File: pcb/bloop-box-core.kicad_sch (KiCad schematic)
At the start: 30 parts, among them J1 Raspberry_Pi_Header, J2 USB_C_Receptacle_USB2.0_16P, J4 Micro_SD_Card_Det1, SW1 Reset, SW2 Boot, U1 ESP32-C5-WROOM-1U, U2 AMS1117-3.3, U3 74LVC125APW

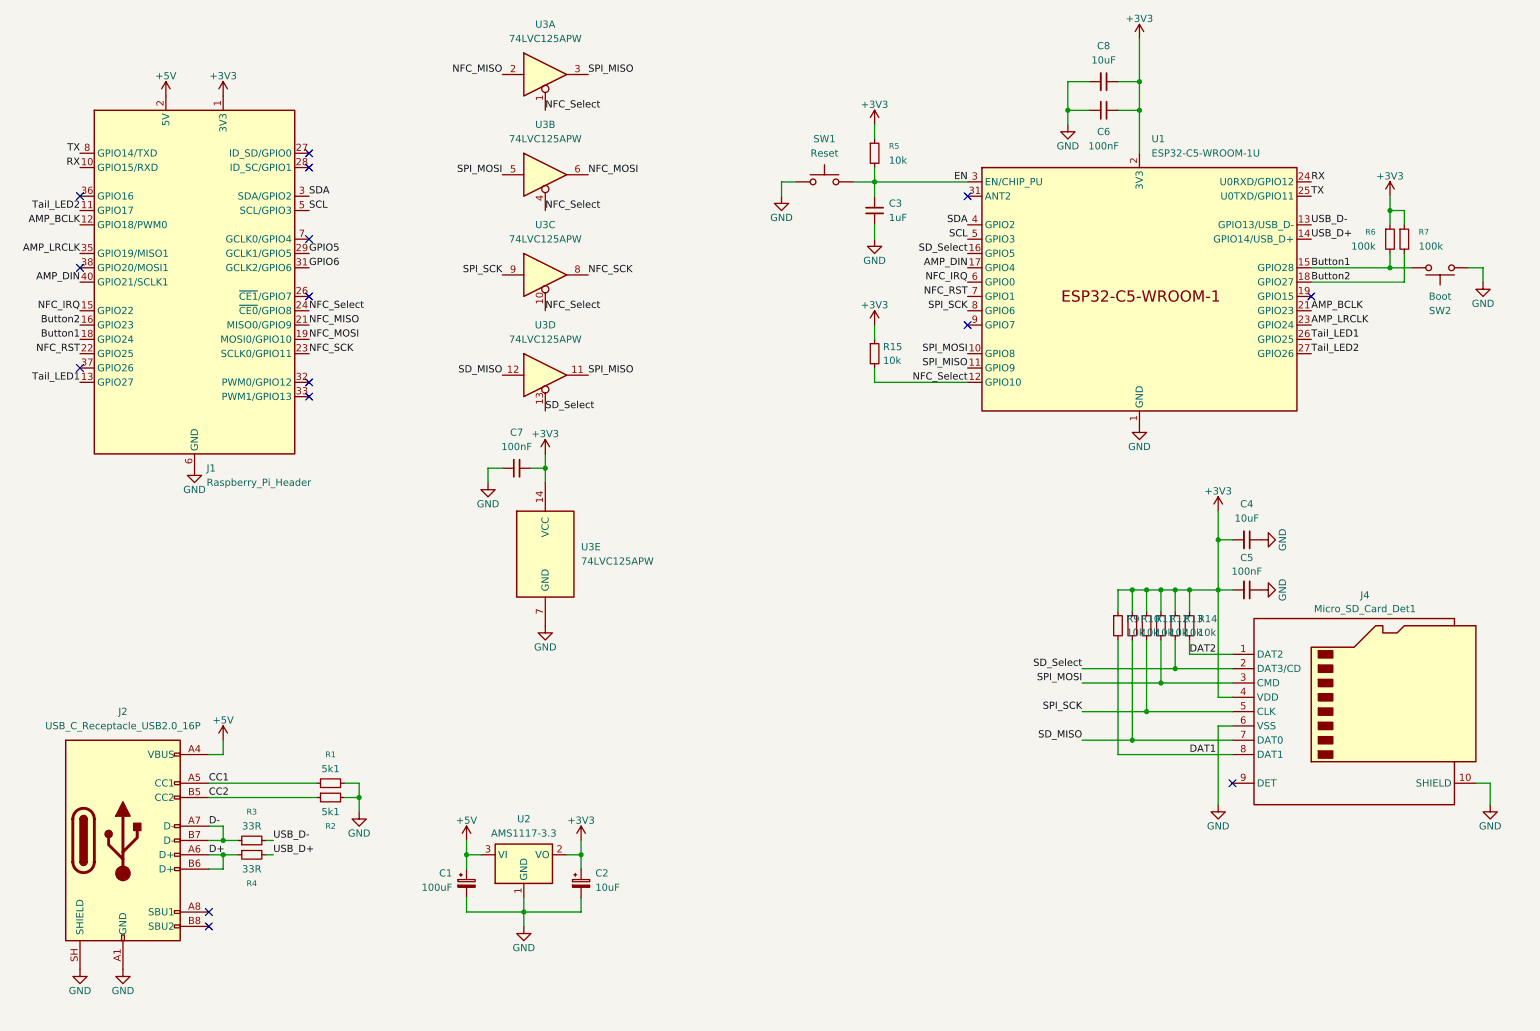
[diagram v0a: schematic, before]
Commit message: feat: trace-routing
All traces are routed
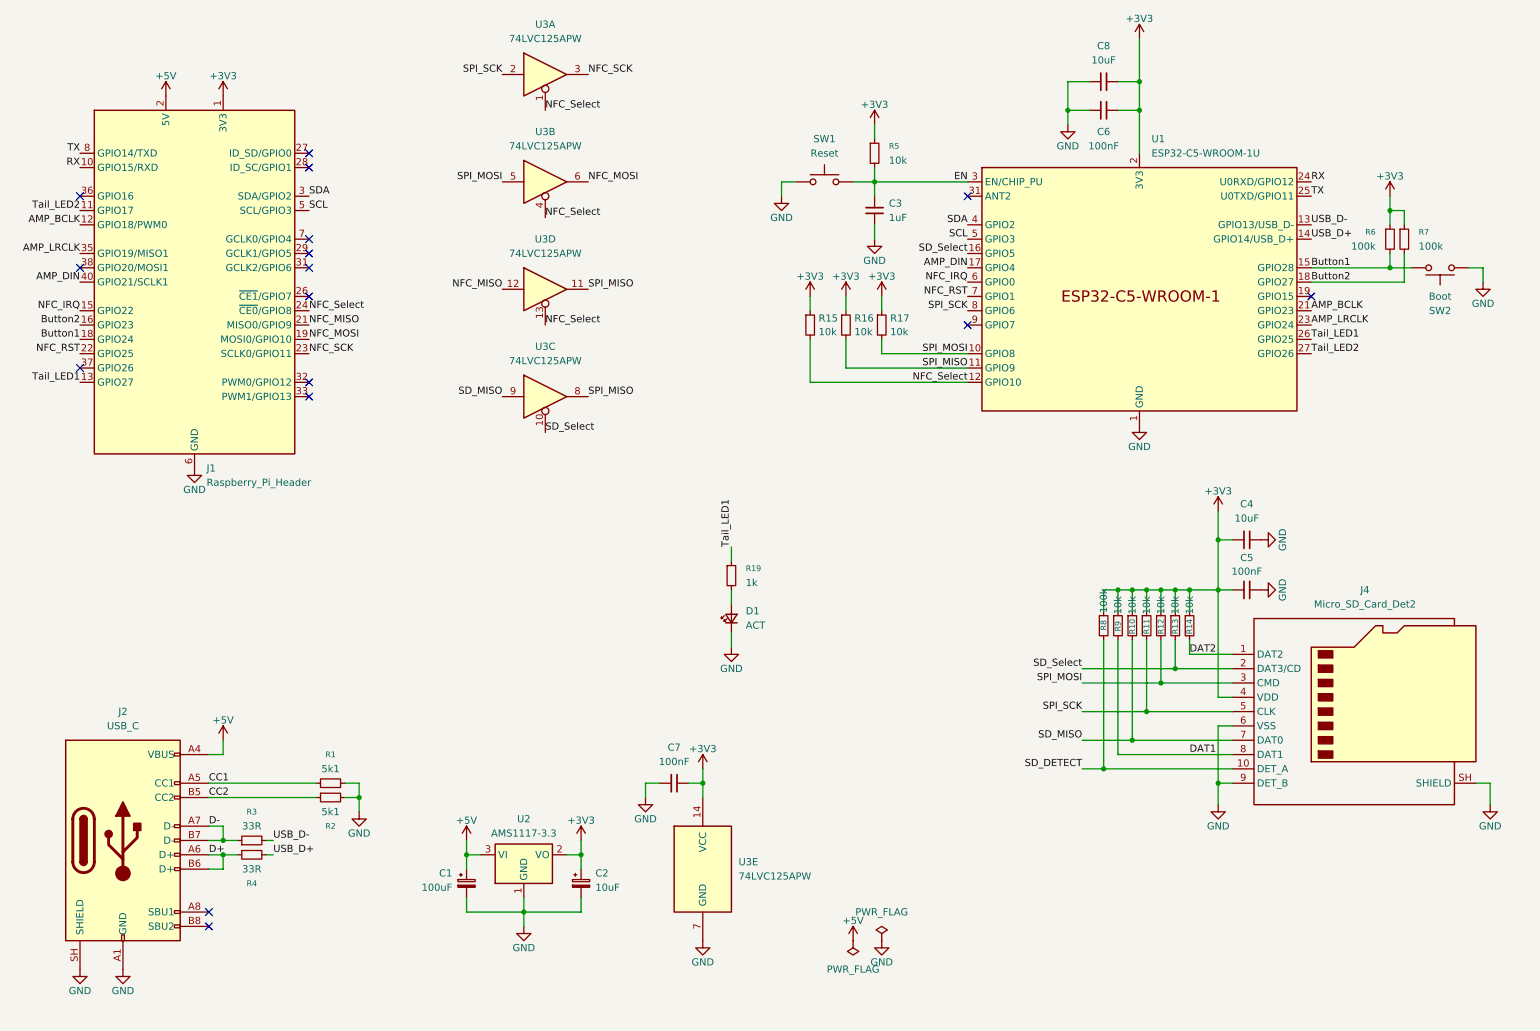
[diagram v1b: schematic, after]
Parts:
- added D1: ACT, LED_SMD:LED_0603_1608Metric, symbol Device:LED_Small
- added R16, R17: 10k, Resistor_SMD:R_0402_1005Metric, symbol Device:R_Small
- added R19: 1k, Resistor_SMD:R_0402_1005Metric, symbol Device:R_Small
- added R8: 100k, Resistor_SMD:R_0402_1005Metric, symbol Device:R_Small
- J2: value USB_C_Receptacle_USB2.0_16P -> USB_C
- J4: value Micro_SD_Card_Det1 -> Micro_SD_Card_Det2; footprint My_Footprints:TF_PUSH_Micro-SD-Connector -> Connector_Card:microSD_HC_Molex_104031-0811; symbol Connector:Micro_SD_Card_Det1 -> Connector:Micro_SD_Card_Det2; LCSC C393941 -> C585350
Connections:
- net +3V3: now also R16.1, R17.1, R8.1
- net GND: now also J4.9 (DET_B), J4.SH (SHIELD), D1.1 (K); no longer J4.10 (SHIELD)
- net NFC_MISO: now also U3.12; no longer U3.2
- net NFC_SCK: now also U3.3; no longer U3.8
- net NFC_Select: now also U3.13; no longer U3.10
- net SD_MISO: now also U3.9; no longer U3.12
- net SD_Select: now also U3.10; no longer U3.13
- net SPI_MISO: now also U3.8, R16.2; no longer U3.3
- net SPI_MOSI: now also R17.2
- net SPI_SCK: now also U3.2; no longer U3.9
- net Tail_LED1: now also R19.1
- net GPIO5: no longer names the net of J1.29 (GCLK1/GPIO5)
- net GPIO6: no longer names the net of J1.31 (GCLK2/GPIO6)
- new net: D1.2 (A), R19.2
- new net SD_DETECT: J4.10 (DET_A), R8.2
- no-connect marks 15 -> 16
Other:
- moved on the sheet: C7, R15, U3B, U3C, U3D, U3E

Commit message: feat: add detect pin for SD-Card
connect SD-Detect to IO7

feat: bottom silkscreen
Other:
- moved on the sheet: C1, C2, C7, D1, R19, U2, U3A, U3B, U3C, U3D, U3E

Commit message: feat: add edge rails
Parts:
- renumbered R19 to R18
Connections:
- net SD_DETECT: now also U1.9 (GPIO7)
- no-connect marks 16 -> 15
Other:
- moved on the sheet: R15, R16, R17
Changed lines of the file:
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@@
 	)
 	(no_connect
-		(at 184.15 73.66)
-	)
-	(no_connect
 		(at 49.53 177.8)
 	)
@@
 	(wire
 		(pts
-			(xy 168.91 68.58) (xy 168.91 71.12)
+			(xy 167.64 68.58) (xy 167.64 71.12)
 		)
 		(stroke
@@
 	(wire
 		(pts
-			(xy 156.21 68.58) (xy 156.21 71.12)
+			(xy 154.94 68.58) (xy 154.94 71.12)
 		)
 		(stroke
@@
 	(wire
 		(pts
-			(xy 156.21 83.82) (xy 184.15 83.82)
+			(xy 154.94 83.82) (xy 184.15 83.82)
 		)
 		(stroke
@@
 	(wire
 		(pts
-			(xy 168.91 78.74) (xy 184.15 78.74)
+			(xy 167.64 78.74) (xy 184.15 78.74)
 		)
 		(stroke
@@
 	(wire
 		(pts
-			(xy 156.21 76.2) (xy 156.21 83.82)
+			(xy 154.94 76.2) (xy 154.94 83.82)
 		)
 		(stroke
@@
 	(wire
 		(pts
-			(xy 162.56 81.28) (xy 184.15 81.28)
+			(xy 161.29 81.28) (xy 184.15 81.28)
 		)
 		(stroke
@@
 	(wire
 		(pts
-			(xy 162.56 76.2) (xy 162.56 81.28)
+			(xy 161.29 76.2) (xy 161.29 81.28)
 		)
 		(stroke
@@
 	(wire
 		(pts
-			(xy 168.91 76.2) (xy 168.91 78.74)
+			(xy 167.64 76.2) (xy 167.64 78.74)
 		)
 		(stroke
@@
 	(wire
 		(pts
-			(xy 162.56 68.58) (xy 162.56 71.12)
+			(xy 161.29 68.58) (xy 161.29 71.12)
 		)
 		(stroke
@@
 		)
 	)
+	(label "SD_DETECT"
+		(at 184.15 73.66 180)
+		(effects
+			(font
+				(size 1.27 1.27)
+			)
+			(justify right bottom)
+		)
+	)
 	(label "NFC_Select"
 		(at 67.31 71.12 0)
@@
 		(lib_name "R_Small_5")
 		(lib_id "Device:R_Small")
-		(at 168.91 73.66 0)
+		(at 167.64 73.66 0)
 		(unit 1)
 		(body_style 1)
@@
 		(fields_autoplaced yes)
 		(property "Reference" "R17"
-			(at 170.4086 72.4479 0)
+			(at 169.1386 72.4479 0)
 			(show_name no)
 			(do_not_autoplace no)
@@
 		)
 		(property "Value" "10k"
-			(at 170.4086 74.8721 0)
+			(at 169.1386 74.8721 0)
 			(show_name no)
 			(do_not_autoplace no)
@@
 		)
 		(property "Footprint" "Resistor_SMD:R_0402_1005Metric"
-			(at 168.91 73.66 0)
+			(at 167.64 73.66 0)
 			(hide yes)
 			(show_name no)
@@
 		)
 		(property "Datasheet" ""
-			(at 168.91 73.66 0)
+			(at 167.64 73.66 0)
 			(hide yes)
 			(show_name no)
@@
 		)
 		(property "Description" ""
-			(at 168.91 73.66 0)
+			(at 167.64 73.66 0)
 			(hide yes)
 			(show_name no)
@@
 		)
 		(property "LCSC" "C25744"
-			(at 168.91 73.66 0)
+			(at 167.64 73.66 0)
 			(hide yes)
 			(show_name no)
@@
 	(symbol
 		(lib_id "power:+3V3")
-		(at 156.21 68.58 0)
+		(at 154.94 68.58 0)
 		(unit 1)
 		(body_style 1)
@@
 		(fields_autoplaced yes)
 		(property "Reference" "#PWR0115"
-			(at 156.21 72.39 0)
+			(at 154.94 72.39 0)
 			(hide yes)
 			(show_name no)
@@
 		)
 		(property "Value" "+3V3"
-			(at 156.21 65.024 0)
+			(at 154.94 65.024 0)
 			(show_name no)
 			(do_not_autoplace no)
@@
 		)
 		(property "Footprint" ""
-			(at 156.21 68.58 0)
+			(at 154.94 68.58 0)
 			(hide yes)
 			(show_name no)
@@
 		)
 		(property "Datasheet" ""
-			(at 156.21 68.58 0)
+			(at 154.94 68.58 0)
 			(hide yes)
 			(show_name no)
@@
 		)
 		(property "Description" "Power symbol creates a global label with name \"+3V3\""
-			(at 156.21 68.58 0)
+			(at 154.94 68.58 0)
 			(hide yes)
 			(show_name no)
@@
 		(dnp no)
 		(fields_autoplaced yes)
-		(property "Reference" "R19"
+		(property "Reference" "R18"
 			(at 167.64 111.7599 0)
 			(show_name no)
@@
 			(project "bloop-box-core"
 				(path "/c58e92c8-e304-41da-860e-e835a4f4fbe5"
-					(reference "R19")
+					(reference "R18")
 					(unit 1)
 				)
@@
 		(lib_name "R_Small_5")
 		(lib_id "Device:R_Small")
-		(at 162.56 73.66 0)
+		(at 161.29 73.66 0)
 		(unit 1)
 		(body_style 1)
@@
 		(fields_autoplaced yes)
 		(property "Reference" "R16"
-			(at 164.0586 72.4479 0)
+			(at 162.7886 72.4479 0)
 			(show_name no)
 			(do_not_autoplace no)
@@
 		)
 		(property "Value" "10k"
-			(at 164.0586 74.8721 0)
+			(at 162.7886 74.8721 0)
 			(show_name no)
 			(do_not_autoplace no)
@@
 		)
 		(property "Footprint" "Resistor_SMD:R_0402_1005Metric"
-			(at 162.56 73.66 0)
+			(at 161.29 73.66 0)
 			(hide yes)
 			(show_name no)
@@
 		)
 		(property "Datasheet" ""
-			(at 162.56 73.66 0)
+			(at 161.29 73.66 0)
 			(hide yes)
 			(show_name no)
@@
 		)
 		(property "Description" ""
-			(at 162.56 73.66 0)
+			(at 161.29 73.66 0)
 			(hide yes)
 			(show_name no)
@@
 		)
 		(property "LCSC" "C25744"
-			(at 162.56 73.66 0)
+			(at 161.29 73.66 0)
 			(hide yes)
 			(show_name no)
@@
 		(lib_name "R_Small_5")
 		(lib_id "Device:R_Small")
-		(at 156.21 73.66 0)
+		(at 154.94 73.66 0)
 		(unit 1)
 		(body_style 1)
@@
 		(fields_autoplaced yes)
 		(property "Reference" "R15"
-			(at 157.7086 72.4479 0)
+			(at 156.4386 72.4479 0)
 			(show_name no)
 			(do_not_autoplace no)
@@
 		)
 		(property "Value" "10k"
-			(at 157.7086 74.8721 0)
+			(at 156.4386 74.8721 0)
 			(show_name no)
 			(do_not_autoplace no)
@@
 		)
 		(property "Footprint" "Resistor_SMD:R_0402_1005Metric"
-			(at 156.21 73.66 0)
+			(at 154.94 73.66 0)
 			(hide yes)
 			(show_name no)
@@
 		)
 		(property "Datasheet" ""
-			(at 156.21 73.66 0)
+			(at 154.94 73.66 0)
 			(hide yes)
 			(show_name no)
@@
 		)
 		(property "Description" ""
-			(at 156.21 73.66 0)
+			(at 154.94 73.66 0)
 			(hide yes)
 			(show_name no)
@@
 		)
 		(property "LCSC" "C25744"
-			(at 156.21 73.66 0)
+			(at 154.94 73.66 0)
 			(hide yes)
 			(show_name no)
@@
 	(symbol
 		(lib_id "power:+3V3")
-		(at 168.91 68.58 0)
+		(at 167.64 68.58 0)
 		(unit 1)
 		(body_style 1)
@@
 		(fields_autoplaced yes)
 		(property "Reference" "#PWR0117"
-			(at 168.91 72.39 0)
+			(at 167.64 72.39 0)
 			(hide yes)
 			(show_name no)
@@
 		)
 		(property "Value" "+3V3"
-			(at 168.91 65.024 0)
+			(at 167.64 65.024 0)
 			(show_name no)
 			(do_not_autoplace no)
@@
 		)
 		(property "Footprint" ""
-			(at 168.91 68.58 0)
+			(at 167.64 68.58 0)
 			(hide yes)
 			(show_name no)
@@
 		)
 		(property "Datasheet" ""
-			(at 168.91 68.58 0)
+			(at 167.64 68.58 0)
 			(hide yes)
 			(show_name no)
@@
 		)
 		(property "Description" "Power symbol creates a global label with name \"+3V3\""
-			(at 168.91 68.58 0)
+			(at 167.64 68.58 0)
 			(hide yes)
 			(show_name no)
@@
 	(symbol
 		(lib_id "power:+3V3")
-		(at 162.56 68.58 0)
+		(at 161.29 68.58 0)
 		(unit 1)
 		(body_style 1)
@@
 		(fields_autoplaced yes)
 		(property "Reference" "#PWR0116"
-			(at 162.56 72.39 0)
+			(at 161.29 72.39 0)
 			(hide yes)
 			(show_name no)
@@
 		)
 		(property "Value" "+3V3"
-			(at 162.56 65.024 0)
+			(at 161.29 65.024 0)
 			(show_name no)
 			(do_not_autoplace no)
@@
 		)
 		(property "Footprint" ""
-			(at 162.56 68.58 0)
+			(at 161.29 68.58 0)
 			(hide yes)
 			(show_name no)
@@
 		)
 		(property "Datasheet" ""
-			(at 162.56 68.58 0)
+			(at 161.29 68.58 0)
 			(hide yes)
 			(show_name no)
@@
 		)
 		(property "Description" "Power symbol creates a global label with name \"+3V3\""
-			(at 162.56 68.58 0)
+			(at 161.29 68.58 0)
 			(hide yes)
 			(show_name no)

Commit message: fix: capacitor values
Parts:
- J1: LCSC C2977589 -> C50980
- renumbered C2 to C1, C1 to C2
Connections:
- net +3V3: now also C2.1; no longer C1.1
- net +5V: now also C1.1; no longer C2.1
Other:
- company: (none) -> Hardware design by Qetesh
- moved on the sheet: C1, C2
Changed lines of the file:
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@@
 		(date "${DATE}")
 		(rev "${VERSION}")
+		(company "Hardware design by Qetesh")
 	)
 	(junction
@@
 	(symbol
 		(lib_id "Device:C_Polarized_Small")
-		(at 111.76 172.72 0)
+		(at 91.44 172.72 0)
 		(unit 1)
 		(body_style 1)
@@
 		(dnp no)
 		(fields_autoplaced yes)
-		(property "Reference" "C2"
-			(at 114.3 170.9038 0)
+		(property "Reference" "C1"
+			(at 88.9 170.9038 0)
 			(show_name no)
 			(do_not_autoplace no)
@@
 					(size 1.27 1.27)
 				)
-				(justify left)
+				(justify right)
 			)
 		)
 		(property "Value" "10uF"
-			(at 114.3 173.4438 0)
+			(at 88.9 173.4438 0)
 			(show_name no)
 			(do_not_autoplace no)
@@
 					(size 1.27 1.27)
 				)
-				(justify left)
+				(justify right)
 			)
 		)
 		(property "Footprint" "Capacitor_Tantalum_SMD:CP_EIA-3216-18_Kemet-A"
-			(at 111.76 172.72 0)
+			(at 91.44 172.72 0)
 			(hide yes)
 			(show_name no)
@@
 		)
 		(property "Datasheet" ""
-			(at 111.76 172.72 0)
+			(at 91.44 172.72 0)
 			(hide yes)
 			(show_name no)
@@
 		)
 		(property "Description" "Polarized capacitor, small symbol"
-			(at 111.76 172.72 0)
+			(at 91.44 172.72 0)
 			(hide yes)
 			(show_name no)
@@
 		)
 		(property "LCSC" "C7171"
-			(at 111.76 172.72 0)
+			(at 91.44 172.72 0)
 			(hide yes)
 			(show_name no)
@@
 			(project "bloop-box-core"
 				(path "/c58e92c8-e304-41da-860e-e835a4f4fbe5"
-					(reference "C2")
+					(reference "C1")
 					(unit 1)
 				)
@@
 	(symbol
 		(lib_id "Device:C_Polarized_Small")
-		(at 91.44 172.72 0)
+		(at 111.76 172.72 0)
 		(unit 1)
 		(body_style 1)
@@
 		(dnp no)
 		(fields_autoplaced yes)
-		(property "Reference" "C1"
-			(at 88.9 170.9038 0)
+		(property "Reference" "C2"
+			(at 114.3 170.9038 0)
 			(show_name no)
 			(do_not_autoplace no)
@@
 					(size 1.27 1.27)
 				)
-				(justify right)
+				(justify left)
 			)
 		)
 		(property "Value" "100uF"
-			(at 88.9 173.4438 0)
+			(at 114.3 173.4438 0)
 			(show_name no)
 			(do_not_autoplace no)
@@
 					(size 1.27 1.27)
 				)
-				(justify right)
+				(justify left)
 			)
 		)
 		(property "Footprint" "Capacitor_Tantalum_SMD:CP_EIA-3528-21_Kemet-B"
-			(at 91.44 172.72 0)
+			(at 111.76 172.72 0)
 			(hide yes)
 			(show_name no)
@@
 		)
 		(property "Datasheet" ""
-			(at 91.44 172.72 0)
+			(at 111.76 172.72 0)
 			(hide yes)
 			(show_name no)
@@
 		)
 		(property "Description" "Polarized capacitor, small symbol"
-			(at 91.44 172.72 0)
+			(at 111.76 172.72 0)
 			(hide yes)
 			(show_name no)
@@
 		)
 		(property "LCSC" "C16133"
-			(at 91.44 172.72 0)
+			(at 111.76 172.72 0)
 			(hide yes)
 			(show_name no)
@@
 			(project "bloop-box-core"
 				(path "/c58e92c8-e304-41da-860e-e835a4f4fbe5"
-					(reference "C1")
+					(reference "C2")
 					(unit 1)
 				)
@@
 			)
 		)
-		(property "LCSC" "C2977589"
+		(property "LCSC" "C50980"
 			(at 46.99 66.04 0)
 			(hide yes)
@@
 					(unit 1)
 				)
+			)
+		)
+	)
+	(symbol
+		(lib_id "Graphic:Logo_Open_Hardware_Small")
+		(at 278.13 175.26 0)
+		(unit 1)
+		(body_style 1)
+		(exclude_from_sim no)
+		(in_bom no)
+		(on_board no)
+		(in_pos_files yes)
+		(dnp no)
+		(fields_autoplaced yes)
+		(property "Reference" "#SYM1"
+			(at 278.13 168.275 0)
+			(hide yes)
+			(show_name no)
+			(do_not_autoplace no)
+			(effects
+				(font
+					(size 1.27 1.27)
+				)
+			)
+		)
+		(property "Value" "Logo_Open_Hardware_Small"
+			(at 278.13 180.975 0)
+			(hide yes)
+			(show_name no)
+			(do_not_autoplace no)
+			(effects
+				(font
+					(size 1.27 1.27)
+				)
+			)
+		)
+		(property "Footprint" "Package_TO_SOT_SMD:SOT-353_SC-70-5"
+			(at 278.13 175.26 0)
+			(hide yes)
+			(show_name no)
+			(do_not_autoplace no)
+			(effects
+				(font
+					(size 1.27 1.27)
+				)
+			)
+		)
+		(property "Datasheet" ""
+			(at 278.13 175.26 0)
+			(hide yes)
+			(show_name no)
+			(do_not_autoplace no)
+			(effects
+				(font
+					(size 1.27 1.27)
+				)
+			)
+		)
+		(property "Description" "Open Hardware logo, small"
+			(at 278.13 175.26 0)
+			(hide yes)
+			(show_name no)
+			(do_not_autoplace no)
+			(effects
+				(font
+					(size 1.27 1.27)
+				)
+			)
+		)
+		(property "Sim.Enable" "0"
+			(at 278.13 175.26 0)
+			(hide yes)
+			(show_name no)
+			(do_not_autoplace no)
+			(effects
+				(font
+					(size 1.27 1.27)
+				)
+			)
+		)
+		(instances
+			(project "bloop-box-core"
+				(path "/c58e92c8-e304-41da-860e-e835a4f4fbe5"
+					(reference "#SYM1")
+					(unit 1)
+				)
